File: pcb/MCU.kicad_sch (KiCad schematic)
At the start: 61 parts, among them J2 Conn_ST_STDC14, J3 Micro_SD_Card, SW1 SW_BLACK, SW2 SW_BLUE, U7 STM32U595ZJTx, Y2 16MHz

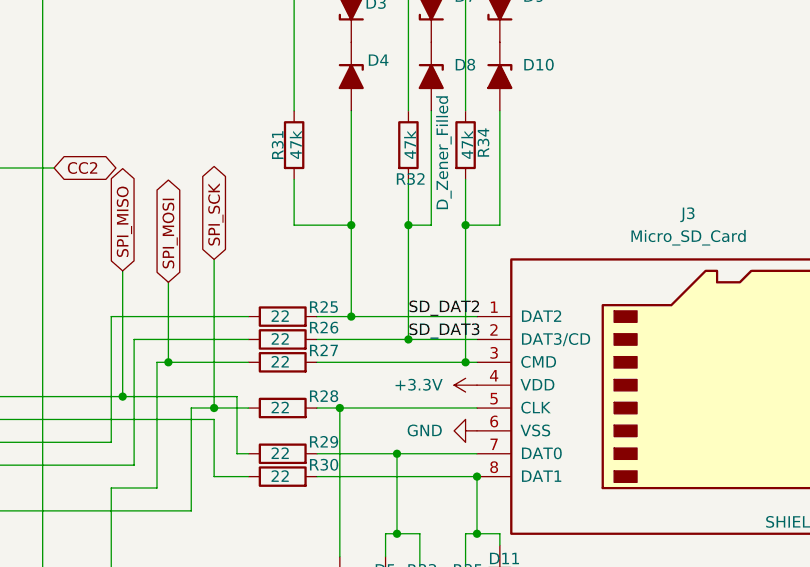
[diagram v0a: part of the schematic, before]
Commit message: fixed erc errors
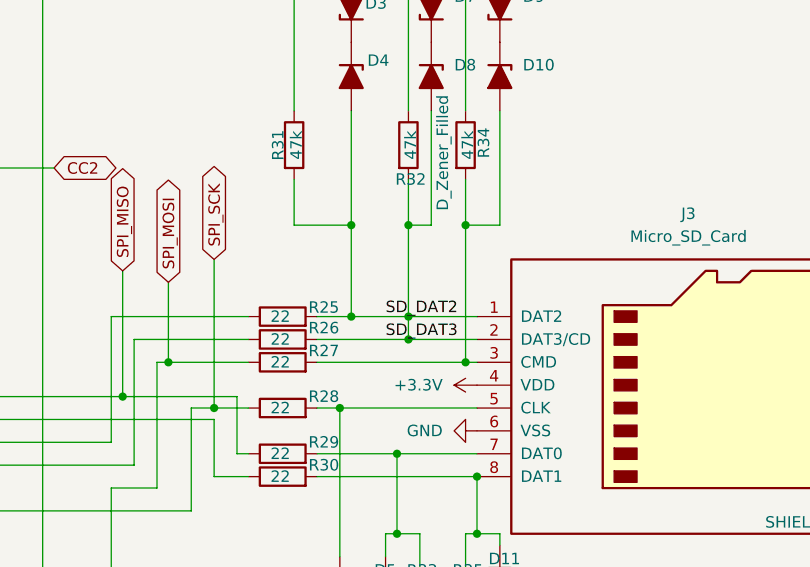
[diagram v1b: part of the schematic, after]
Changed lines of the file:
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@@
 	)
 	(junction
+		(at 289.56 163.83)
+		(diameter 0)
+		(color 0 0 0 0)
+	)
+	(junction
 		(at 35.56 166.37)
 		(diameter 0)
@@
 	(wire
 		(pts
+			(xy 289.56 163.83) (xy 297.18 163.83)
+		)
+		(stroke
+			(width 0)
+			(type default)
+		)
+	)
+	(wire
+		(pts
 			(xy 290.83 205.74) (xy 294.64 205.74)
 		)
@@
 	(wire
 		(pts
-			(xy 289.56 153.67) (xy 289.56 166.37)
+			(xy 289.56 153.67) (xy 289.56 163.83)
 		)
 		(stroke
@@
 	(wire
 		(pts
-			(xy 279.4 163.83) (xy 297.18 163.83)
+			(xy 279.4 163.83) (xy 289.56 163.83)
 		)
 		(stroke
@@
 	(wire
 		(pts
+			(xy 289.56 163.83) (xy 289.56 166.37)
+		)
+		(stroke
+			(width 0)
+			(type default)
+		)
+	)
+	(wire
+		(pts
 			(xy 142.24 99.06) (xy 78.74 99.06)
 		)
@@
 	)
 	(label "SD_DAT3"
-		(at 289.56 166.37 0)
+		(at 287.02 166.37 0)
 		(effects
 			(font
@@
 	)
 	(label "SD_DAT2"
-		(at 289.56 163.83 0)
+		(at 287.02 163.83 0)
 		(effects
 			(font

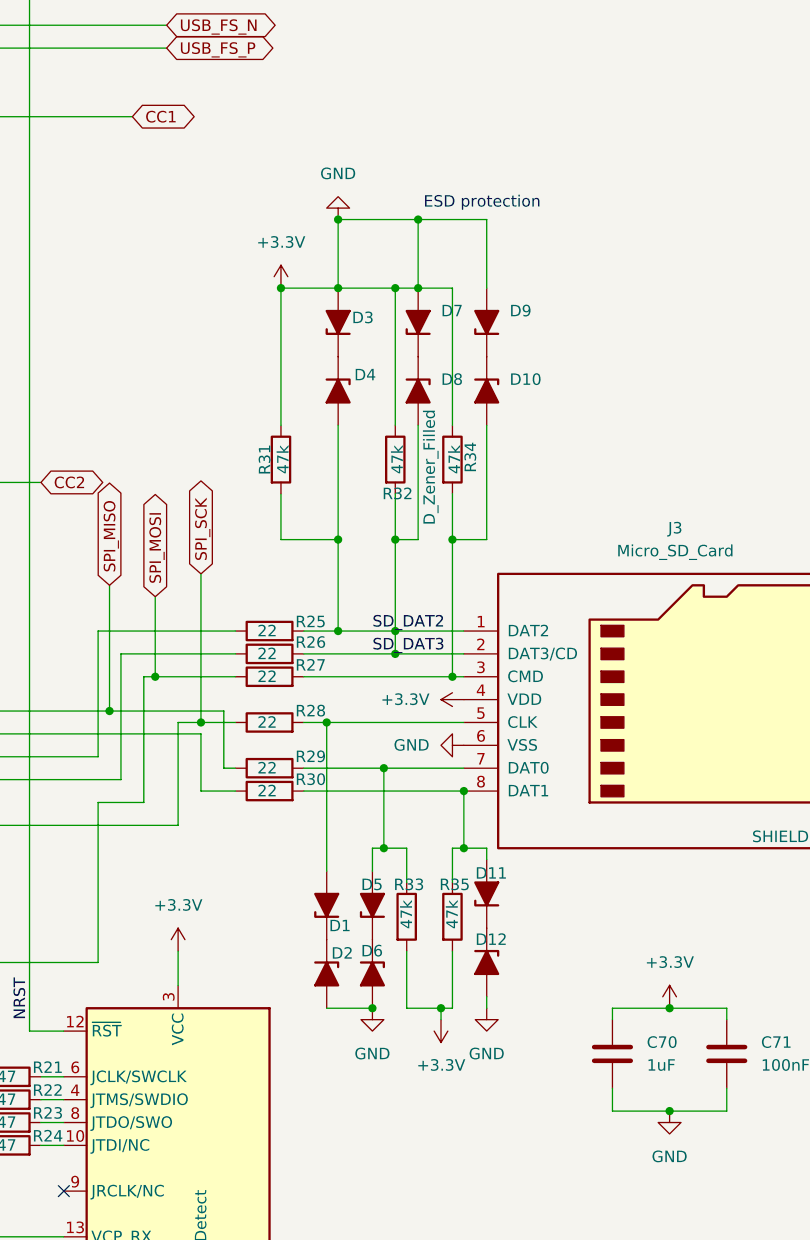
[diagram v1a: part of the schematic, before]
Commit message: removed sd card esd protection
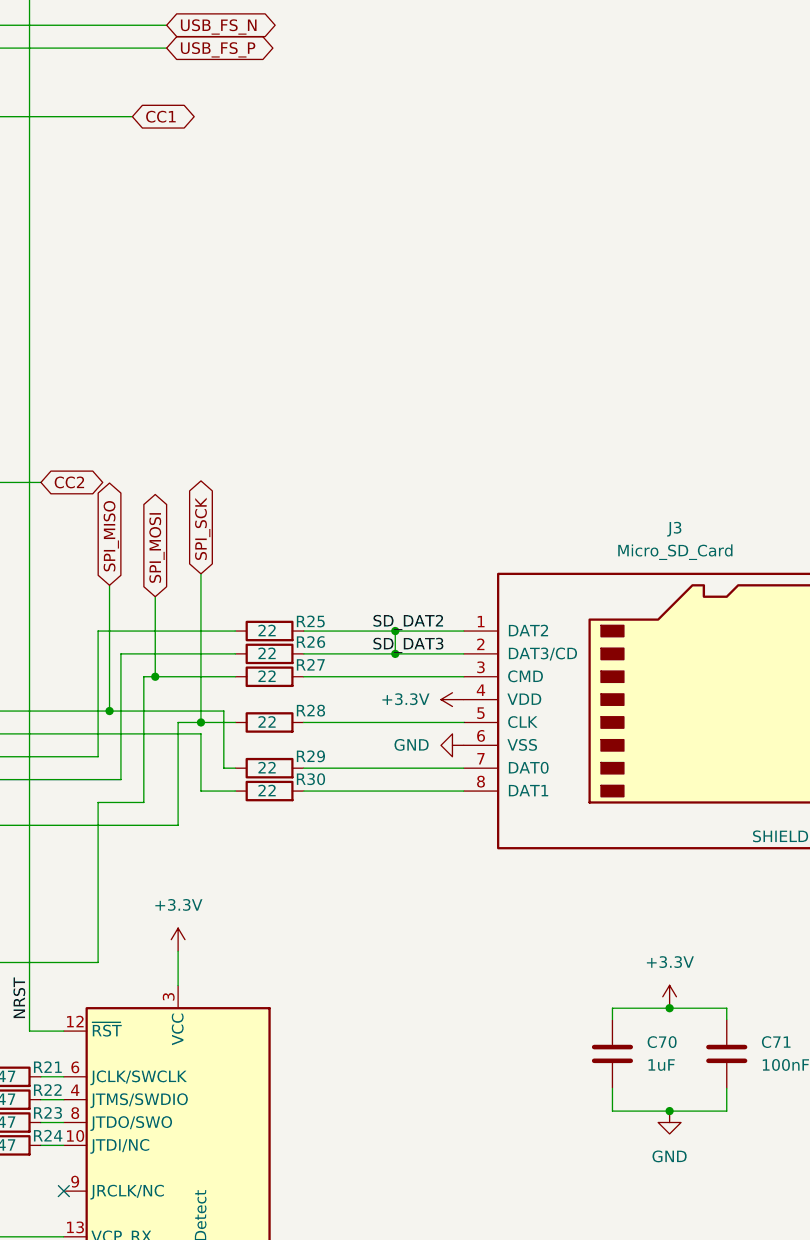
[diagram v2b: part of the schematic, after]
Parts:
- removed D1, D10, D11, D12, D2, D3, D4, D5, D6, D7, D8, D9: D_Zener_Filled, symbol Device:D_Zener_Filled
- removed R31, R32, R33, R34, R35: 47k, symbol Device:R
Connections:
- net +3.3V: no longer C50.2, C51.2, C52.2, C53.2, C54.2, C55.2, C56.2, C57.2, C58.2, C59.2, C60.1, C61.1, C62.2, C63.2, C64.2, C65.2, C66.2, C67.2, C68.2, C69.1, C70.2, C71.2, C75.2, C76.2, J2.5 (GND), J2.7 (GND), J3.6 (VSS), J3.SH (SHIELD), R20.1, SW1.2, U7.107 (VSS), U7.120 (VSS), U7.130 (VSS), U7.143 (VSS), U7.16 (VSS), U7.30 (VSSA), U7.31 (VREF-), U7.38 (VSS), U7.51 (VSS), U7.61 (VSS), U7.71 (VSS), U7.83 (VSS), U7.94 (VSS), Y2.2 (G), Y2.4 (G)
- new net GND: C50.2, C51.2, C52.2, C53.2, C54.2, C55.2, C56.2, C57.2, C58.2, C59.2, C60.1, C61.1, C62.2, C63.2, C64.2, C65.2, C66.2, C67.2, C68.2, C69.1, C70.2, C71.2, C75.2, C76.2, J2.5 (GND), J2.7 (GND), J3.6 (VSS), J3.SH (SHIELD), R20.1, SW1.2, U7.107 (VSS), U7.120 (VSS), U7.130 (VSS), U7.143 (VSS), U7.16 (VSS), U7.30 (VSSA), U7.31 (VREF-), U7.38 (VSS), U7.51 (VSS), U7.61 (VSS), U7.71 (VSS), U7.83 (VSS), U7.94 (VSS), Y2.2 (G), Y2.4 (G)
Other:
- note removed: "ESD protection"

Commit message: pcb: satisfy ERC warnings and errors
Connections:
- net MCU VCAP: no longer names the net of C66.1, U7.70 (VCAP)
- net MCU_STLINK_JCLK: no longer names the net of R21.1, U7.109 (PA14)
- net MCU_STLINK_JTDO: no longer names the net of R23.1, U7.133 (PB3)
- net MCU_STLINK_JTMS: no longer names the net of R22.1, U7.105 (PA13)
- net MCU_VCP_RX: no longer names the net of J2.13 (VCP_RX), U7.102 (PA10)
- net MCU_VCP_TX: no longer names the net of J2.14 (VCP_TX), U7.101 (PA9)
- net NRST: no longer names the net of C69.2, J2.12 (~{RST}), SW1.1, U7.25 (NRST)
- net SD_DAT1: no longer names the net of R30.1, U7.99 (PC9)
- net SD_DAT2: no longer names the net of J3.1 (DAT2), J3.2 (DAT3/CD), R25.2, R26.2
- net SP1_MISO renamed SPI1_MISO
- net SP1_MOSI renamed SPI1_MOSI
- net SP1_SCK renamed SPI1_SCK
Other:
- note added: "MCU_STLINK_JCLK"
- note added: "MCU_STLINK_JTDI"
- note added: "MCU_STLINK_JTDO"
- note added: "MCU_STLINK_JTMS"
- note added: "MCU_VCP_RX"
- note added: "MCU_VCP_TX"
- note added: "NRST"
- note added: "SD_DAT0"
- note added: "SD_DAT1"
- note added: "SD_DAT2"
- note added: "SD_DAT3"
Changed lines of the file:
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@@
 		(title "MCU design")
 	)
+	(text "MCU_STLINK_JTMS"
+		(exclude_from_sim no)
+		(at 217.17 101.6 0)
+		(effects
+			(font
+				(size 1.27 1.27)
+			)
+			(justify left bottom)
+		)
+	)
+	(text "NRST"
+		(exclude_from_sim no)
+		(at 248.92 207.01 90)
+		(effects
+			(font
+				(size 1.27 1.27)
+			)
+			(justify left bottom)
+		)
+	)
+	(text "SD_DAT0"
+		(exclude_from_sim no)
+		(at 217.17 172.72 0)
+		(effects
+			(font
+				(size 1.27 1.27)
+			)
+			(justify left bottom)
+		)
+	)
 	(text "FORCE BOOT TO LOW, LOAD FIRMWARE INSTEAD\n"
 		(exclude_from_sim no)
@@
 		)
 	)
+	(text "SD_DAT1"
+		(exclude_from_sim no)
+		(at 217.17 175.26 0)
+		(effects
+			(font
+				(size 1.27 1.27)
+			)
+			(justify left bottom)
+		)
+	)
+	(text "MCU_VCP_RX"
+		(exclude_from_sim no)
+		(at 217.17 93.98 0)
+		(effects
+			(font
+				(size 1.27 1.27)
+			)
+			(justify left bottom)
+		)
+	)
+	(text "MCU_STLINK_JTDI"
+		(exclude_from_sim no)
+		(at 217.17 106.68 0)
+		(effects
+			(font
+				(size 1.27 1.27)
+			)
+			(justify left bottom)
+		)
+	)
+	(text "SD_DAT2"
+		(exclude_from_sim no)
+		(at 287.02 163.83 0)
+		(effects
+			(font
+				(size 1.27 1.27)
+			)
+			(justify left bottom)
+		)
+	)
+	(text "MCU_STLINK_JTDO"
+		(exclude_from_sim no)
+		(at 217.17 119.38 0)
+		(effects
+			(font
+				(size 1.27 1.27)
+			)
+			(justify left bottom)
+		)
+	)
+	(text "MCU_STLINK_JCLK"
+		(exclude_from_sim no)
+		(at 217.17 104.14 0)
+		(effects
+			(font
+				(size 1.27 1.27)
+			)
+			(justify left bottom)
+		)
+	)
+	(text "MCU_VCP_TX"
+		(exclude_from_sim no)
+		(at 217.17 91.44 0)
+		(effects
+			(font
+				(size 1.27 1.27)
+			)
+			(justify left bottom)
+		)
+	)
+	(text "SD_DAT3"
+		(exclude_from_sim no)
+		(at 287.02 166.37 0)
+		(effects
+			(font
+				(size 1.27 1.27)
+			)
+			(justify left bottom)
+		)
+	)
 	(junction
 		(at 204.47 38.1)
@@
 	)
 	(junction
-		(at 217.17 147.32)
-		(diameter 0)
-		(color 0 0 0 0)
-	)
-	(junction
 		(at 52.07 158.75)
 		(diameter 0)
@@
 	(wire
 		(pts
-			(xy 208.28 147.32) (xy 217.17 147.32)
-		)
-		(stroke
-			(width 0)
-			(type default)
-		)
-	)
-	(wire
-		(pts
 			(xy 241.3 101.6) (xy 217.17 101.6)
 		)
@@
 		)
 	)
-	(label "SD_DAT0"
-		(at 217.17 172.72 0)
-		(effects
-			(font
-				(size 1.27 1.27)
-			)
-			(justify left bottom)
-		)
-	)
-	(label "MCU_VDDUSB"
-		(at 217.17 40.64 270)
-		(effects
-			(font
-				(size 1.27 1.27)
-			)
-			(justify right bottom)
-		)
-	)
-	(label "MCU_VREF-"
-		(at 146.05 76.2 0)
-		(effects
-			(font
-				(size 1.27 1.27)
-			)
-			(justify left bottom)
-		)
-	)
-	(label "MCU_VCP_RX"
-		(at 217.17 93.98 0)
-		(effects
-			(font
-				(size 1.27 1.27)
-			)
-			(justify left bottom)
-		)
-	)
-	(label "MCU_VCP_TX"
-		(at 217.17 91.44 0)
-		(effects
-			(font
-				(size 1.27 1.27)
-			)
-			(justify left bottom)
-		)
-	)
-	(label "SD_DAT3"
-		(at 287.02 166.37 0)
-		(effects
-			(font
-				(size 1.27 1.27)
-			)
-			(justify left bottom)
-		)
-	)
-	(label "MCU_STLINK_JTDI"
-		(at 217.17 106.68 0)
-		(effects
-			(font
-				(size 1.27 1.27)
-			)
-			(justify left bottom)
-		)
-	)
-	(label "NRST"
-		(at 248.92 207.01 90)
-		(effects
-			(font
-				(size 1.27 1.27)
-			)
-			(justify left bottom)
-		)
-	)
-	(label "MCU_VSS"
-		(at 173.99 243.84 0)
-		(effects
-			(font
-				(size 1.27 1.27)
-			)
-			(justify left bottom)
-		)
-	)
-	(label "MCU_VREF+"
-		(at 151.13 72.39 90)
-		(effects
-			(font
-				(size 1.27 1.27)
-			)
-			(justify left bottom)
-		)
-	)
-	(label "MCU_STLINK_JTMS"
-		(at 218.44 101.6 0)
-		(effects
-			(font
-				(size 1.27 1.27)
-			)
-			(justify left bottom)
-		)
-	)
-	(label "MCU_STLINK_JTDO"
-		(at 217.17 119.38 0)
-		(effects
-			(font
-				(size 1.27 1.27)
-			)
-			(justify left bottom)
-		)
-	)
-	(label "MCU_STLINK_JCLK"
-		(at 217.17 104.14 0)
-		(effects
-			(font
-				(size 1.27 1.27)
-			)
-			(justify left bottom)
-		)
-	)
-	(label "SD_DAT2"
-		(at 287.02 163.83 0)
-		(effects
-			(font
-				(size 1.27 1.27)
-			)
-			(justify left bottom)
-		)
-	)
-	(label "SD_DAT1"
-		(at 217.17 175.26 0)
-		(effects
-			(font
-				(size 1.27 1.27)
-			)
-			(justify left bottom)
-		)
-	)
-	(label "MCU VCAP"
-		(at 146.05 220.98 0)
-		(effects
-			(font
-				(size 1.27 1.27)
-			)
-			(justify left bottom)
-		)
-	)
-	(global_label "SP1_MOSI"
+	(global_label "SPI1_MOSI"
 		(shape bidirectional)
 		(at 226.06 86.36 0)
@@
 		)
 		(property "Intersheetrefs" "${INTERSHEET_REFS}"
-			(at 239.4093 86.36 0)
+			(at 240.0141 86.36 0)
 			(hide yes)
 			(show_name no)
@@
 		)
 	)
-	(global_label "SP1_MISO"
+	(global_label "SPI1_MISO"
 		(shape bidirectional)
 		(at 226.06 83.82 0)
@@
 		)
 		(property "Intersheetrefs" "${INTERSHEET_REFS}"
-			(at 239.4093 83.82 0)
+			(at 240.0141 83.82 0)
 			(hide yes)
 			(show_name no)
@@
 		)
 	)
-	(global_label "SP1_SCK"
+	(global_label "SPI1_SCK"
 		(shape input)
 		(at 226.06 71.12 0)
@@
 		)
 		(property "Intersheetrefs" "${INTERSHEET_REFS}"
-			(at 237.4513 71.12 0)
+			(at 238.0561 71.12 0)
 			(hide yes)
 			(show_name no)

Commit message: added mcu rgb led
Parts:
- added D1: LED_ARGB, SON4_APTF1616LSEEZGKQBKC_KNB, symbol APTF1616LSEEZGKQBKC:APTF1616LSEEZGKQBKC
- added R31, R32: 22, symbol Device:R
- added R33: 51, symbol Device:R
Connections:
- net GND: now also D1.1
- net at U7.1 (PE2): now also R33.2
- net at U7.141 (PE0): now also R31.2
- net at U7.142 (PE1): now also R32.2
- new net: D1.4, R31.1
- new net: D1.2, R33.1
- new net: D1.3, R32.1
- no-connect marks 69 -> 66

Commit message: layout prep
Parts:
- C50, C51, C52, C53, C54, C55, C56, C57, C58, C59, C60, C61, C62, C63, C64, C65, C66, C67, C68, C69, C70, C71, C74, C75, C76: footprint (none) -> Capacitor_SMD:C_0805_2012Metric_Pad1.18x1.45mm_HandSolder
- D1: footprint SON4_APTF1616LSEEZGKQBKC_KNB -> LED_ARGB:SON4_APTF1616LSEEZGKQBKC_KNB
- J2: footprint (none) -> Connector_PinHeader_1.27mm:PinHeader_2x07_P1.27mm_Vertical_SMD
- R20, R21, R22, R23, R24, R25, R26, R27, R28, R29, R30, R31, R32, R33, R42, R43: footprint (none) -> Resistor_SMD:R_0805_2012Metric_Pad1.20x1.40mm_HandSolder
- SW2: footprint SW_Push_1P1T_NO_CK_KSC6xxG -> Button_Switch_SMD:SW_Push_1P1T_NO_CK_KSC6xxG
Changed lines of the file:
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@@
 			)
 		)
-		(property "Footprint" ""
+		(property "Footprint" "Capacitor_SMD:C_0805_2012Metric_Pad1.18x1.45mm_HandSolder"
 			(at 48.26 157.7848 0)
 			(hide yes)
@@
 			)
 		)
-		(property "Footprint" ""
+		(property "Footprint" "Capacitor_SMD:C_0805_2012Metric_Pad1.18x1.45mm_HandSolder"
 			(at 48.26 131.1148 0)
 			(hide yes)
@@
 			)
 		)
-		(property "Footprint" ""
+		(property "Footprint" "Resistor_SMD:R_0805_2012Metric_Pad1.20x1.40mm_HandSolder"
 			(at 246.38 220.218 90)
 			(hide yes)
@@
 			)
 		)
-		(property "Footprint" ""
+		(property "Footprint" "Capacitor_SMD:C_0805_2012Metric_Pad1.18x1.45mm_HandSolder"
 			(at 48.26 171.7548 0)
 			(hide yes)
@@
 			)
 		)
-		(property "Footprint" ""
+		(property "Footprint" "Capacitor_SMD:C_0805_2012Metric_Pad1.18x1.45mm_HandSolder"
 			(at 48.26 122.2248 0)
 			(hide yes)
@@
 			)
 		)
-		(property "Footprint" ""
+		(property "Footprint" "Capacitor_SMD:C_0805_2012Metric_Pad1.18x1.45mm_HandSolder"
 			(at 48.26 145.0848 0)
 			(hide yes)
@@
 			)
 		)
-		(property "Footprint" ""
+		(property "Footprint" "Capacitor_SMD:C_0805_2012Metric_Pad1.18x1.45mm_HandSolder"
 			(at 205.4352 45.72 0)
 			(hide yes)
@@
 			)
 		)
-		(property "Footprint" ""
+		(property "Footprint" "Resistor_SMD:R_0805_2012Metric_Pad1.20x1.40mm_HandSolder"
 			(at 121.92 107.188 90)
 			(hide yes)
@@
 			)
 		)
-		(property "Footprint" ""
+		(property "Footprint" "Capacitor_SMD:C_0805_2012Metric_Pad1.18x1.45mm_HandSolder"
 			(at 139.3952 64.77 0)
 			(hide yes)
@@
 			)
 		)
-		(property "Footprint" ""
+		(property "Footprint" "Capacitor_SMD:C_0805_2012Metric_Pad1.18x1.45mm_HandSolder"
 			(at 48.26 151.4348 0)
 			(hide yes)
@@
 			)
 		)
-		(property "Footprint" ""
+		(property "Footprint" "Resistor_SMD:R_0805_2012Metric_Pad1.20x1.40mm_HandSolder"
 			(at 246.38 215.138 90)
 			(hide yes)
@@
 			)
 		)
-		(property "Footprint" ""
+		(property "Footprint" "Resistor_SMD:R_0805_2012Metric_Pad1.20x1.40mm_HandSolder"
 			(at 275.59 170.688 90)
 			(hide yes)
@@
 			)
 		)
-		(property "Footprint" ""
+		(property "Footprint" "Resistor_SMD:R_0805_2012Metric_Pad1.20x1.40mm_HandSolder"
 			(at 82.042 270.51 90)
 			(hide yes)
@@
 			)
 		)
-		(property "Footprint" ""
+		(property "Footprint" "Capacitor_SMD:C_0805_2012Metric_Pad1.18x1.45mm_HandSolder"
 			(at 48.26 198.4248 0)
 			(hide yes)
@@
 			)
 		)
-		(property "Footprint" ""
+		(property "Footprint" "Resistor_SMD:R_0805_2012Metric_Pad1.20x1.40mm_HandSolder"
 			(at 142.24 179.578 90)
 			(hide yes)
@@
 			)
 		)
-		(property "Footprint" ""
+		(property "Footprint" "Resistor_SMD:R_0805_2012Metric_Pad1.20x1.40mm_HandSolder"
 			(at 275.59 180.848 90)
 			(hide yes)
@@
 			)
 		)
-		(property "Footprint" ""
+		(property "Footprint" "Resistor_SMD:R_0805_2012Metric_Pad1.20x1.40mm_HandSolder"
 			(at 275.59 183.388 90)
 			(hide yes)
@@
 			)
 		)
-		(property "Footprint" ""
+		(property "Footprint" "Resistor_SMD:R_0805_2012Metric_Pad1.20x1.40mm_HandSolder"
 			(at 142.24 189.738 90)
 			(hide yes)
@@
 			)
 		)
-		(property "Footprint" ""
+		(property "Footprint" "Resistor_SMD:R_0805_2012Metric_Pad1.20x1.40mm_HandSolder"
 			(at 246.38 222.758 90)
 			(hide yes)
@@
 			)
 		)
-		(property "Footprint" ""
+		(property "Footprint" "Capacitor_SMD:C_0805_2012Metric_Pad1.18x1.45mm_HandSolder"
 			(at 314.6552 214.63 0)
 			(hide yes)
@@
 			)
 		)
-		(property "Footprint" ""
+		(property "Footprint" "Capacitor_SMD:C_0805_2012Metric_Pad1.18x1.45mm_HandSolder"
 			(at 116.84 77.7748 0)
 			(hide yes)
@@
 			)
 		)
-		(property "Footprint" ""
+		(property "Footprint" "Capacitor_SMD:C_0805_2012Metric_Pad1.18x1.45mm_HandSolder"
 			(at 261.62 77.1652 0)
 			(hide yes)
@@
 			)
 		)
-		(property "Footprint" "SW_Push_1P1T_NO_CK_KSC6xxG"
+		(property "Footprint" "Button_Switch_SMD:SW_Push_1P1T_NO_CK_KSC6xxG"
 			(at 78.74 246.38 0)
 			(hide yes)
@@
 			)
 		)
-		(property "Footprint" ""
+		(property "Footprint" "Capacitor_SMD:C_0805_2012Metric_Pad1.18x1.45mm_HandSolder"
 			(at 327.3552 214.63 0)
 			(hide yes)
@@
 			)
 		)
-		(property "Footprint" ""
+		(property "Footprint" "Capacitor_SMD:C_0805_2012Metric_Pad1.18x1.45mm_HandSolder"
 			(at 140.6652 232.41 0)
 			(hide yes)
@@
 			)
 		)
-		(property "Footprint" ""
+		(property "Footprint" "Resistor_SMD:R_0805_2012Metric_Pad1.20x1.40mm_HandSolder"
 			(at 275.59 168.148 90)
 			(hide yes)
@@
 			)
 		)
-		(property "Footprint" ""
+		(property "Footprint" "Capacitor_SMD:C_0805_2012Metric_Pad1.18x1.45mm_HandSolder"
 			(at 148.2852 46.99 0)
 			(hide yes)
@@
 			)
 		)
-		(property "Footprint" ""
+		(property "Footprint" "Capacitor_SMD:C_0805_2012Metric_Pad1.18x1.45mm_HandSolder"
 			(at 116.84 89.2048 0)
 			(hide yes)
@@
 			)
 		)
-		(property "Footprint" ""
+		(property "Footprint" "Capacitor_SMD:C_0805_2012Metric_Pad1.18x1.45mm_HandSolder"
 			(at 48.26 178.1048 0)
 			(hide yes)
@@
 			)
 		)
-		(property "Footprint" ""
+		(property "Footprint" "Capacitor_SMD:C_0805_2012Metric_Pad1.18x1.45mm_HandSolder"
 			(at 126.6952 64.77 0)
 			(hide yes)
@@
 			)
 		)
-		(property "Footprint" ""
+		(property "Footprint" "Capacitor_SMD:C_0805_2012Metric_Pad1.18x1.45mm_HandSolder"
 			(at 59.3852 273.05 0)
 			(hide yes)
@@
 			)
 		)
-		(property "Footprint" ""
+		(property "Footprint" "Connector_PinHeader_1.27mm:PinHeader_2x07_P1.27mm_Vertical_SMD"
 			(at 265.43 220.98 0)
 			(hide yes)
@@
 			)
 		)
-		(property "Footprint" "SON4_APTF1616LSEEZGKQBKC_KNB"
+		(property "Footprint" "LED_ARGB:SON4_APTF1616LSEEZGKQBKC_KNB"
 			(at 91.44 182.88 0)
 			(hide yes)
@@
 			)
 		)
-		(property "Footprint" ""
+		(property "Footprint" "Capacitor_SMD:C_0805_2012Metric_Pad1.18x1.45mm_HandSolder"
 			(at 124.1552 39.37 0)
 			(hide yes)
@@
 			)
 		)
-		(property "Footprint" ""
+		(property "Footprint" "Resistor_SMD:R_0805_2012Metric_Pad1.20x1.40mm_HandSolder"
 			(at 69.85 262.128 90)
 			(hide yes)
@@
 			)
 		)
-		(property "Footprint" ""
+		(property "Footprint" "Capacitor_SMD:C_0805_2012Metric_Pad1.18x1.45mm_HandSolder"
 			(at 48.26 137.4648 0)
 			(hide yes)
@@
 			)
 		)
-		(property "Footprint" ""
+		(property "Footprint" "Resistor_SMD:R_0805_2012Metric_Pad1.20x1.40mm_HandSolder"
 			(at 142.24 184.658 90)
 			(hide yes)
@@
 			)
 		)
-		(property "Footprint" ""
+		(property "Footprint" "Resistor_SMD:R_0805_2012Metric_Pad1.20x1.40mm_HandSolder"
 			(at 246.38 217.678 90)
 			(hide yes)
@@
 			)
 		)
-		(property "Footprint" ""
+		(property "Footprint" "Capacitor_SMD:C_0805_2012Metric_Pad1.18x1.45mm_HandSolder"
 			(at 48.26 165.4048 0)
 			(hide yes)
@@
 			)
 		)
-		(property "Footprint" ""
+		(property "Footprint" "Resistor_SMD:R_0805_2012Metric_Pad1.20x1.40mm_HandSolder"
 			(at 275.59 165.608 90)
 			(hide yes)
@@
 			)
 		)
-		(property "Footprint" ""
+		(property "Footprint" "Capacitor_SMD:C_0805_2012Metric_Pad1.18x1.45mm_HandSolder"
 			(at 48.26 185.7248 0)
 			(hide yes)
@@
 			)
 		)
-		(property "Footprint" ""
+		(property "Footprint" "Capacitor_SMD:C_0805_2012Metric_Pad1.18x1.45mm_HandSolder"
 			(at 136.8552 39.37 0)
 			(hide yes)
@@
 			)
 		)
-		(property "Footprint" ""
+		(property "Footprint" "Capacitor_SMD:C_0805_2012Metric_Pad1.18x1.45mm_HandSolder"
 			(at 48.26 113.3348 0)
 			(hide yes)
@@
 			)
 		)
-		(property "Footprint" ""
+		(property "Footprint" "Resistor_SMD:R_0805_2012Metric_Pad1.20x1.40mm_HandSolder"
 			(at 275.59 175.768 90)
 			(hide yes)

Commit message: updates labels
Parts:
- renumbered C76 to C50, C75 to C51, C50 to C52, C51 to C53, C52 to C54, C53 to C55, C54 to C56, C55 to C57, C56 to C58, C57 to C59, C58 to C60, C59 to C61, C74 to C62, C60 to C63, C61 to C64, C62 to C65, C63 to C66, C64 to C67, C65 to C68, C66 to C69, C67 to C70, C68 to C71, C69 to C72, C70 to C73, C71 to C74, D1 to D3, J2 to J3, J3 to J4, R43 to R36, R42 to R37, R20 to R38, R31 to R39, R32 to R40, R33 to R41, R21 to R42, R22 to R43, R23 to R44, R24 to R45, R25 to R46, R26 to R47, R27 to R48, R28 to R49, R29 to R50, R30 to R51, SW2 to SW1, SW1 to SW2
